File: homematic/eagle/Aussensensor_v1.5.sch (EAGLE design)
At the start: 44 parts, among them IC1 Atmega 328P, IC2 MAX1724, IC3 MAX44009, IC4 TSL256FN, IC5 BMP180, IC6 BME280, IC7 DS18B20, M1 CC1101_WIRELES_MODULE, T1 IRML6344

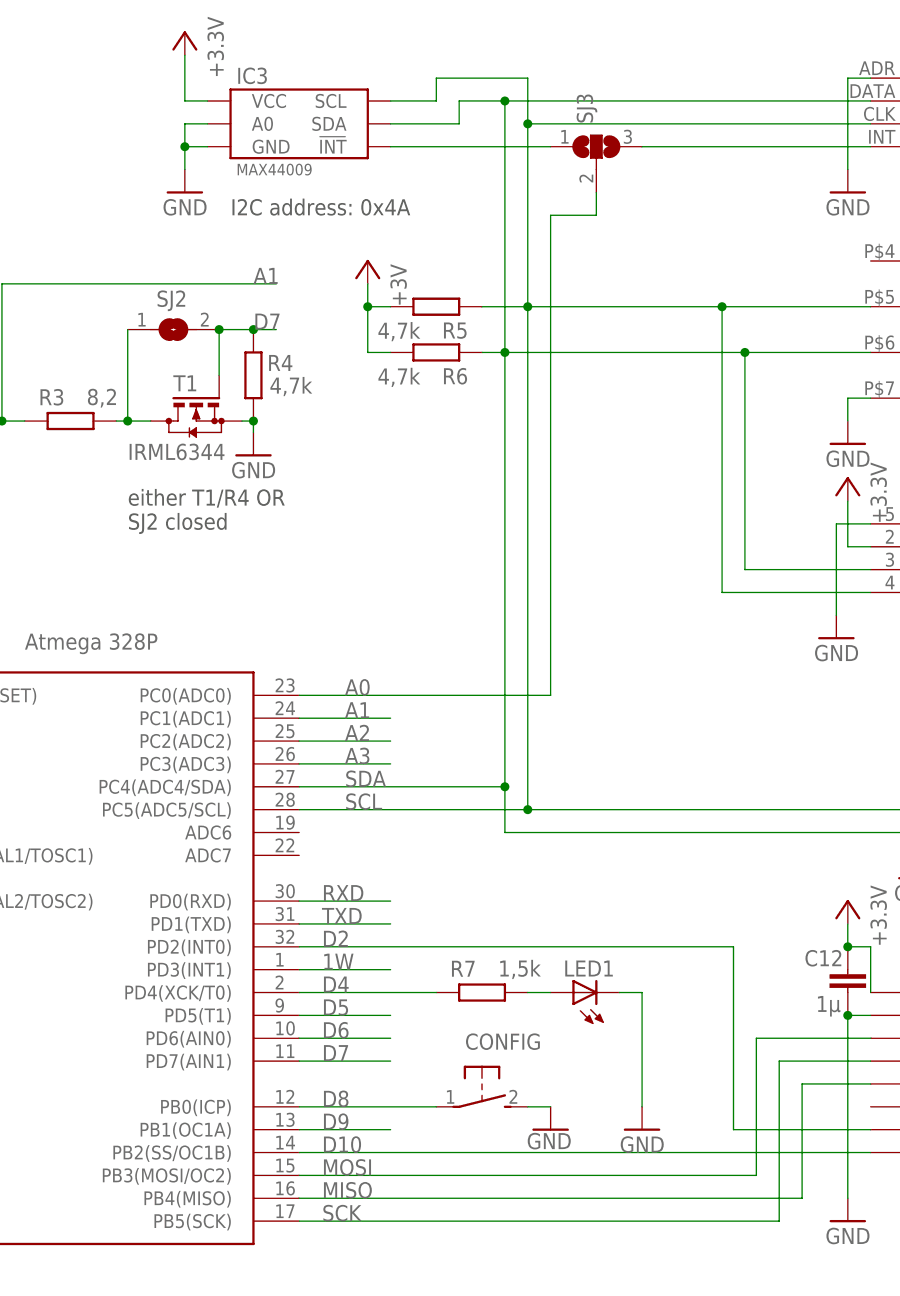
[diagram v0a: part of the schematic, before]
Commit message: Changed compared to previous version: - all vias diameter 0.7, drill 0,4 mm - moved vias for buffer capacitor C3 and C11 - improved layout for C6 - R9 (pull up for CSN) added
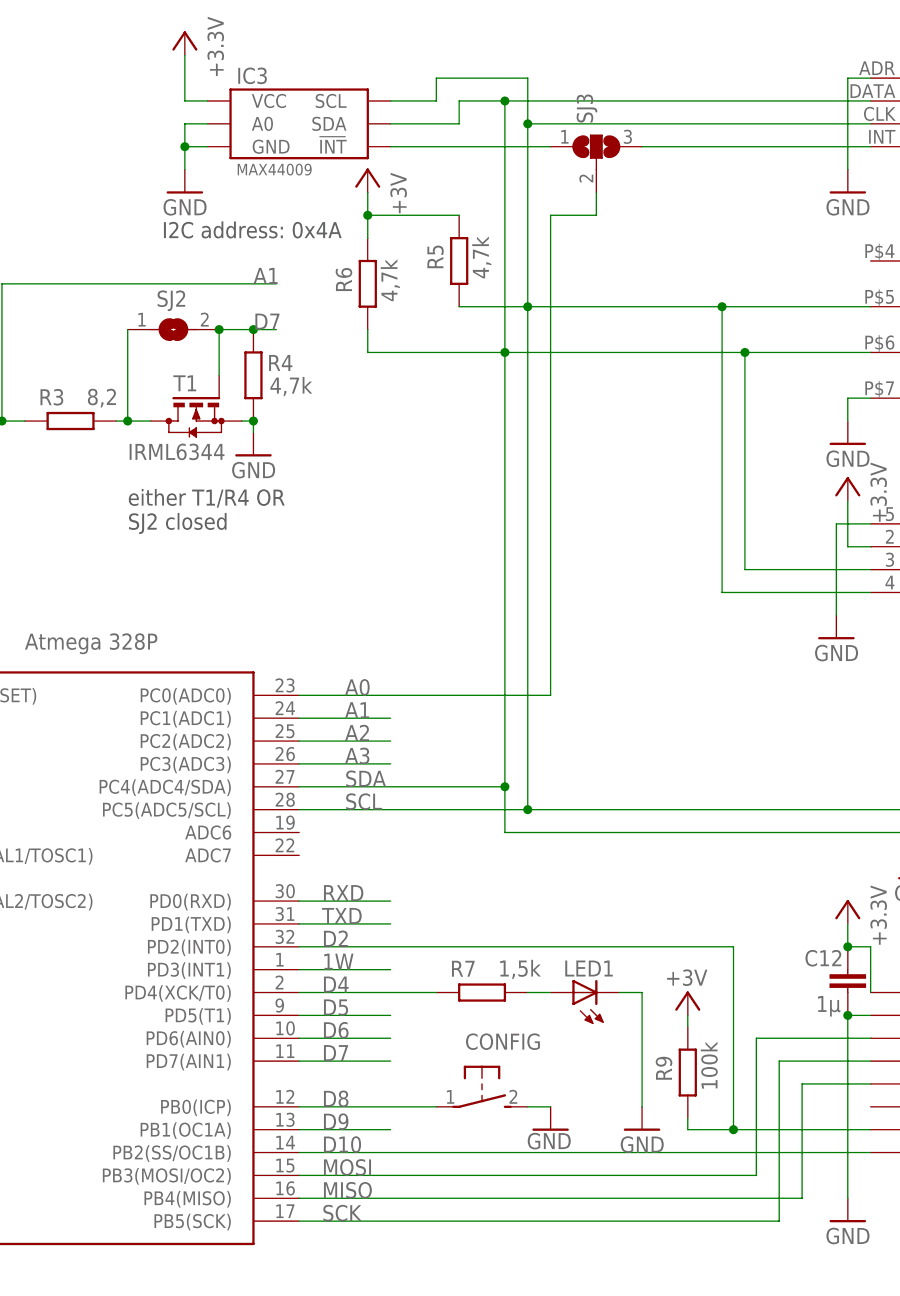
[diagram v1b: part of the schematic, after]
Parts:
- added R9: 100k, rcl:R-EU_M0805
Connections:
- net +3.3V: now also R9.2
- net D2: now also R9.1
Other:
- moved on the sheet: R5, R6
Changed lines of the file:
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@@
 <setting verticaltext="up"/>
 </settings>
-<grid distance="0.1" unitdist="inch" unit="mil" style="lines" multiple="1" display="no" altdistance="0.01" altunitdist="inch" altunit="inch"/>
+<grid distance="50" unitdist="mil" unit="mil" style="lines" multiple="1" display="no" altdistance="0.01" altunitdist="inch" altunit="inch"/>
 <layers>
 <layer number="1" name="Top" color="4" fill="1" visible="no" active="no"/>
@@
 <part name="SJ3" library="jumper" deviceset="SJ2W" device=""/>
 <part name="IC4" library="TSL256x" deviceset="TSL256*" device="FN"/>
+<part name="R9" library="rcl" deviceset="R-EU_" device="M0805" value="100k"/>
+<part name="P+14" library="supply1" deviceset="+5V" device="" value="+3V"/>
 </parts>
 <sheets>
@@
 <text x="120.65" y="124.46" size="1.778" layer="97" rot="MR180">either T1/R4 OR
 SJ2 closed</text>
-<text x="132.08" y="154.94" size="1.778" layer="97">I2C address: 0x4A</text>
+<text x="124.46" y="152.4" size="1.778" layer="97">I2C address: 0x4A</text>
 </plain>
 <instances>
@@
 <instance part="GND15" gate="1" x="254" y="129.54" rot="MR0"/>
 <instance part="GND16" gate="1" x="200.66" y="129.54" rot="MR0"/>
-<instance part="R6" gate="G$1" x="154.94" y="139.7" smashed="yes" rot="R180">
-<attribute name="NAME" x="158.496" y="137.9474" size="1.778" layer="95" rot="R180"/>
-<attribute name="VALUE" x="153.162" y="137.922" size="1.778" layer="96" rot="R180"/>
-</instance>
-<instance part="R5" gate="G$1" x="154.94" y="144.78" smashed="yes" rot="R180">
-<attribute name="NAME" x="158.496" y="143.0274" size="1.778" layer="95" rot="R180"/>
-<attribute name="VALUE" x="153.162" y="143.002" size="1.778" layer="96" rot="R180"/>
-</instance>
-<instance part="P+6" gate="1" x="147.32" y="149.86" rot="MR0"/>
+<instance part="R6" gate="G$1" x="147.32" y="147.32" smashed="yes" rot="R90">
+<attribute name="NAME" x="145.5674" y="146.304" size="1.778" layer="95" rot="R90"/>
+<attribute name="VALUE" x="150.622" y="145.288" size="1.778" layer="96" rot="R90"/>
+</instance>
+<instance part="R5" gate="G$1" x="157.48" y="149.86" smashed="yes" rot="R90">
+<attribute name="NAME" x="155.7274" y="148.844" size="1.778" layer="95" rot="R90"/>
+<attribute name="VALUE" x="160.782" y="147.828" size="1.778" layer="96" rot="R90"/>
+</instance>
+<instance part="P+6" gate="1" x="147.32" y="160.02" rot="MR0"/>
 <instance part="GND18" gate="1" x="236.22" y="157.48" rot="MR0"/>
 <instance part="GND19" gate="1" x="200.66" y="157.48" rot="MR0"/>
@@
 <attribute name="NAME" x="208.28" y="173.99" size="1.778" layer="95" rot="MR0" align="bottom-right"/>
 <attribute name="VALUE" x="228.6" y="157.48" size="1.27" layer="96" rot="MR0"/>
+</instance>
+<instance part="R9" gate="G$1" x="182.88" y="59.69" smashed="yes" rot="R90">
+<attribute name="NAME" x="181.1274" y="58.674" size="1.778" layer="95" rot="R90"/>
+<attribute name="VALUE" x="186.182" y="57.658" size="1.778" layer="96" rot="R90"/>
+</instance>
+<instance part="P+14" gate="1" x="182.88" y="68.58" smashed="yes" rot="MR0">
+<attribute name="VALUE" x="180.34" y="71.12" size="1.778" layer="96" rot="MR180"/>
 </instance>
 </instances>
@@
 <wire x1="187.96" y1="53.34" x2="203.2" y2="53.34" width="0.1524" layer="91"/>
 <label x="142.24" y="73.66" size="1.778" layer="95"/>
+<pinref part="R9" gate="G$1" pin="1"/>
+<wire x1="182.88" y1="54.61" x2="182.88" y2="53.34" width="0.1524" layer="91"/>
+<wire x1="182.88" y1="53.34" x2="187.96" y2="53.34" width="0.1524" layer="91"/>
+<junction x="187.96" y="53.34"/>
 </segment>
 <segment>
@@
 <pinref part="R6" gate="G$1" pin="1"/>
 <wire x1="189.23" y1="139.7" x2="162.56" y2="139.7" width="0.1524" layer="91"/>
-<wire x1="162.56" y1="139.7" x2="160.02" y2="139.7" width="0.1524" layer="91"/>
+<wire x1="162.56" y1="139.7" x2="147.32" y2="139.7" width="0.1524" layer="91"/>
+<wire x1="147.32" y1="139.7" x2="147.32" y2="142.24" width="0.1524" layer="91"/>
 <label x="144.78" y="91.44" size="1.778" layer="95"/>
 <pinref part="IC6" gate="IC" pin="SDI"/>
@@
 <wire x1="139.7" y1="88.9" x2="165.1" y2="88.9" width="0.1524" layer="91"/>
 <pinref part="R5" gate="G$1" pin="1"/>
-<wire x1="165.1" y1="144.78" x2="160.02" y2="144.78" width="0.1524" layer="91"/>
+<wire x1="165.1" y1="144.78" x2="157.48" y2="144.78" width="0.1524" layer="91"/>
 <label x="144.78" y="88.9" size="1.778" layer="95"/>
 <pinref part="IC6" gate="IC" pin="SCK"/>
@@
 <segment>
 <pinref part="R5" gate="G$1" pin="2"/>
-<wire x1="149.86" y1="144.78" x2="147.32" y2="144.78" width="0.1524" layer="91"/>
-<wire x1="147.32" y1="144.78" x2="147.32" y2="139.7" width="0.1524" layer="91"/>
+<wire x1="157.48" y1="154.94" x2="147.32" y2="154.94" width="0.1524" layer="91"/>
+<wire x1="147.32" y1="154.94" x2="147.32" y2="152.4" width="0.1524" layer="91"/>
 <pinref part="R6" gate="G$1" pin="2"/>
-<wire x1="147.32" y1="139.7" x2="149.86" y2="139.7" width="0.1524" layer="91"/>
 <pinref part="P+6" gate="1" pin="+5V"/>
-<wire x1="147.32" y1="144.78" x2="147.32" y2="147.32" width="0.1524" layer="91"/>
-<junction x="147.32" y="144.78"/>
+<wire x1="147.32" y1="154.94" x2="147.32" y2="157.48" width="0.1524" layer="91"/>
+<junction x="147.32" y="154.94"/>
 </segment>
 <segment>
@@
 <wire x1="127" y1="167.64" x2="127" y2="172.72" width="0.1524" layer="91"/>
 </segment>
-</net>
+<segment>
+<pinref part="P+14" gate="1" pin="+5V"/>
+<pinref part="R9" gate="G$1" pin="2"/>
+<wire x1="182.88" y1="66.04" x2="182.88" y2="64.77" width="0.1524" layer="91"/>
+</segment>
+</net>

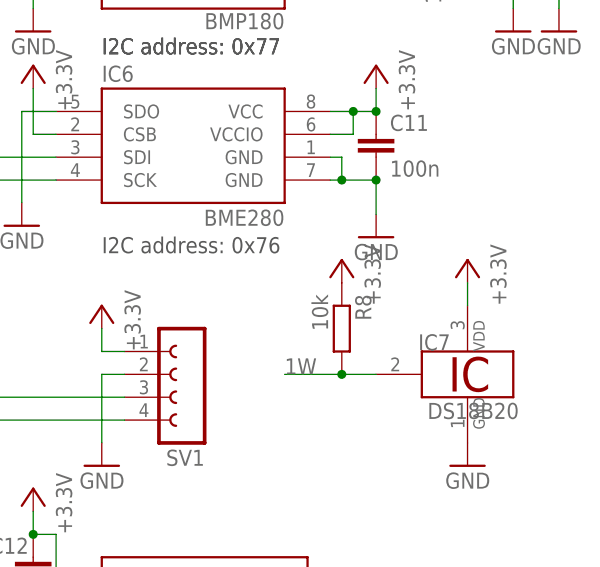
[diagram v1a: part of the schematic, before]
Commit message: replaced 10k by 4k7 for DS18x20 in Aussensensor v1.4 and v1.5
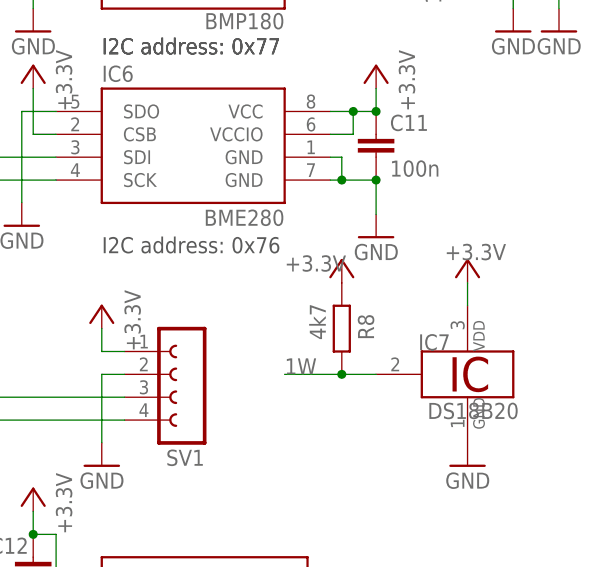
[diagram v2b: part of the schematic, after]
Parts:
- R8: value 10k -> 4k7
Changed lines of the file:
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@@
 <setting verticaltext="up"/>
 </settings>
-<grid distance="50" unitdist="mil" unit="mil" style="lines" multiple="1" display="no" altdistance="0.01" altunitdist="inch" altunit="inch"/>
+<grid distance="0.1" unitdist="inch" unit="inch" style="lines" multiple="1" display="no" altdistance="0.01" altunitdist="inch" altunit="inch"/>
 <layers>
 <layer number="1" name="Top" color="4" fill="1" visible="no" active="no"/>
@@
 <part name="P+11" library="supply1" deviceset="+5V" device="" value="+3.3V"/>
 <part name="GND21" library="supply1" deviceset="GND" device=""/>
-<part name="R8" library="rcl" deviceset="R-EU_" device="M0805" value="10k"/>
+<part name="R8" library="rcl" deviceset="R-EU_" device="M0805" value="4k7"/>
 <part name="P+12" library="supply1" deviceset="+5V" device="" value="+3.3V"/>
 <part name="C12" library="rcl" deviceset="C-EU" device="C0805" value="1µ"/>
@@
 <instance part="IC7" gate="P" x="248.92" y="91.44" smashed="yes"/>
 <instance part="IC7" gate="_1W" x="243.84" y="91.44" smashed="yes"/>
-<instance part="P+11" gate="1" x="248.92" y="104.14" rot="MR0"/>
+<instance part="P+11" gate="1" x="248.92" y="104.14" smashed="yes" rot="MR0">
+<attribute name="VALUE" x="246.38" y="104.14" size="1.778" layer="96"/>
+</instance>
 <instance part="GND21" gate="1" x="248.92" y="81.28" rot="MR0"/>
-<instance part="R8" gate="G$1" x="234.95" y="96.52" rot="R270"/>
-<instance part="P+12" gate="1" x="234.95" y="104.14" rot="MR0"/>
+<instance part="R8" gate="G$1" x="234.95" y="96.52" smashed="yes" rot="R270">
+<attribute name="NAME" x="238.5314" y="95.25" size="1.778" layer="95" rot="R90"/>
+<attribute name="VALUE" x="233.172" y="95.25" size="1.778" layer="96" rot="R90"/>
+</instance>
+<instance part="P+12" gate="1" x="234.95" y="104.14" smashed="yes" rot="MR0">
+<attribute name="VALUE" x="228.6" y="102.87" size="1.778" layer="96"/>
+</instance>
 <instance part="C12" gate="G$1" x="200.66" y="71.12" smashed="yes">
 <attribute name="NAME" x="195.834" y="71.501" size="1.778" layer="95"/>

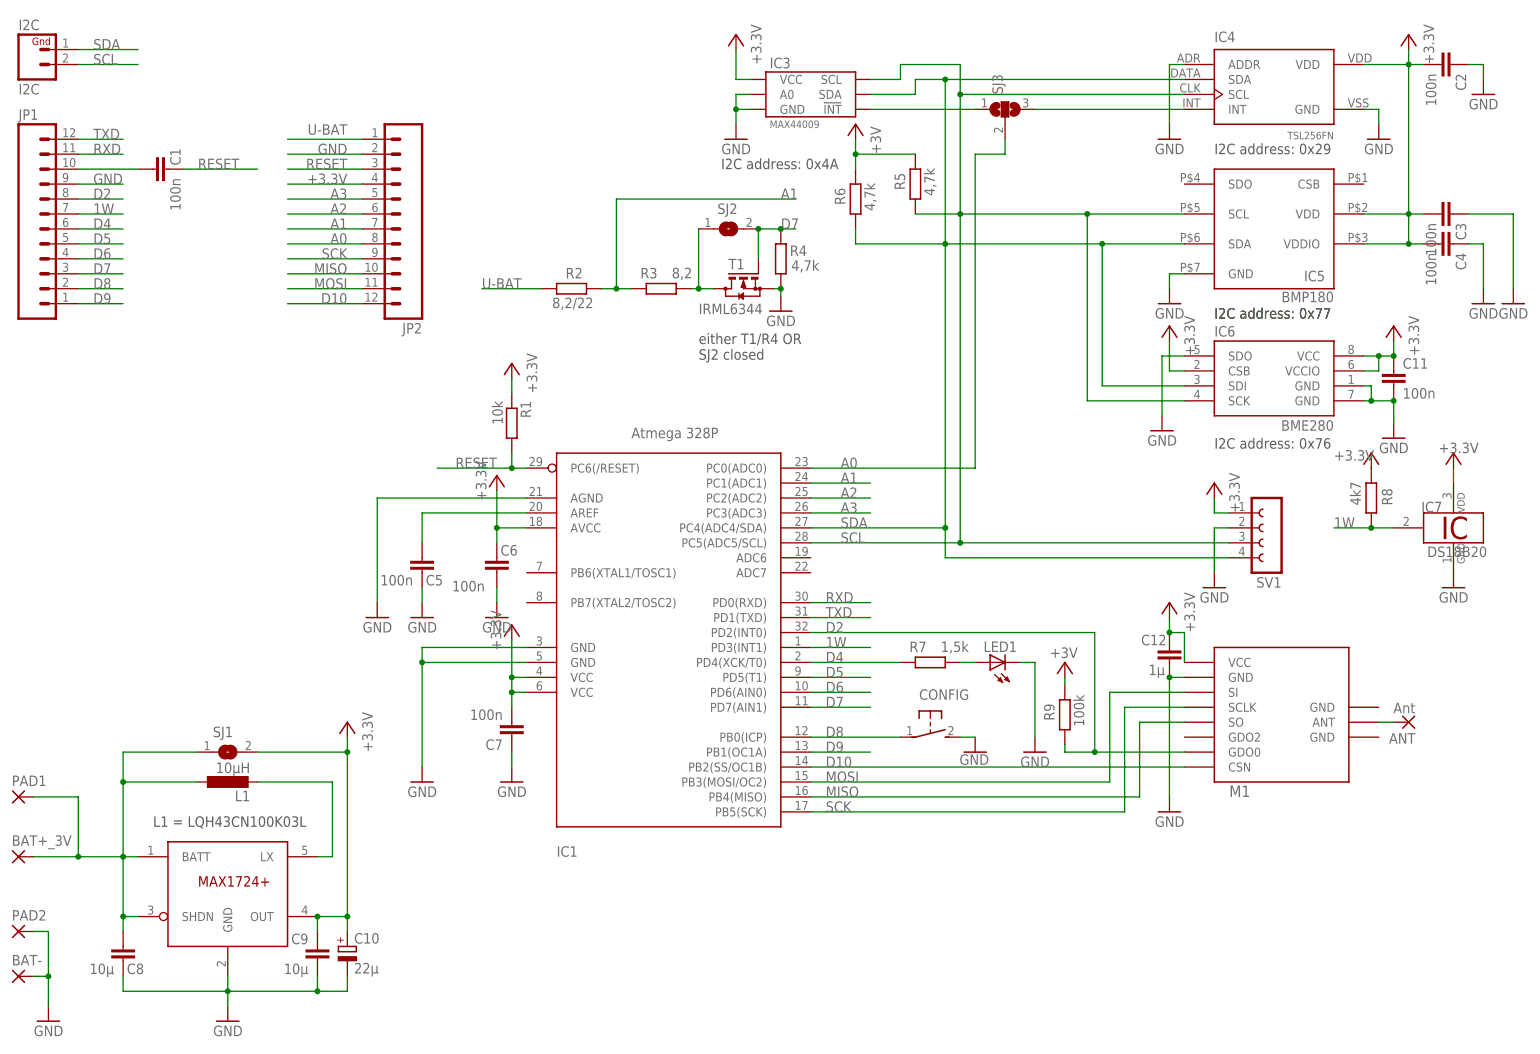
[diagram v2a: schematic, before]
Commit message: replace Aussensensor v1.5 with a better readable schematic (no layout change)
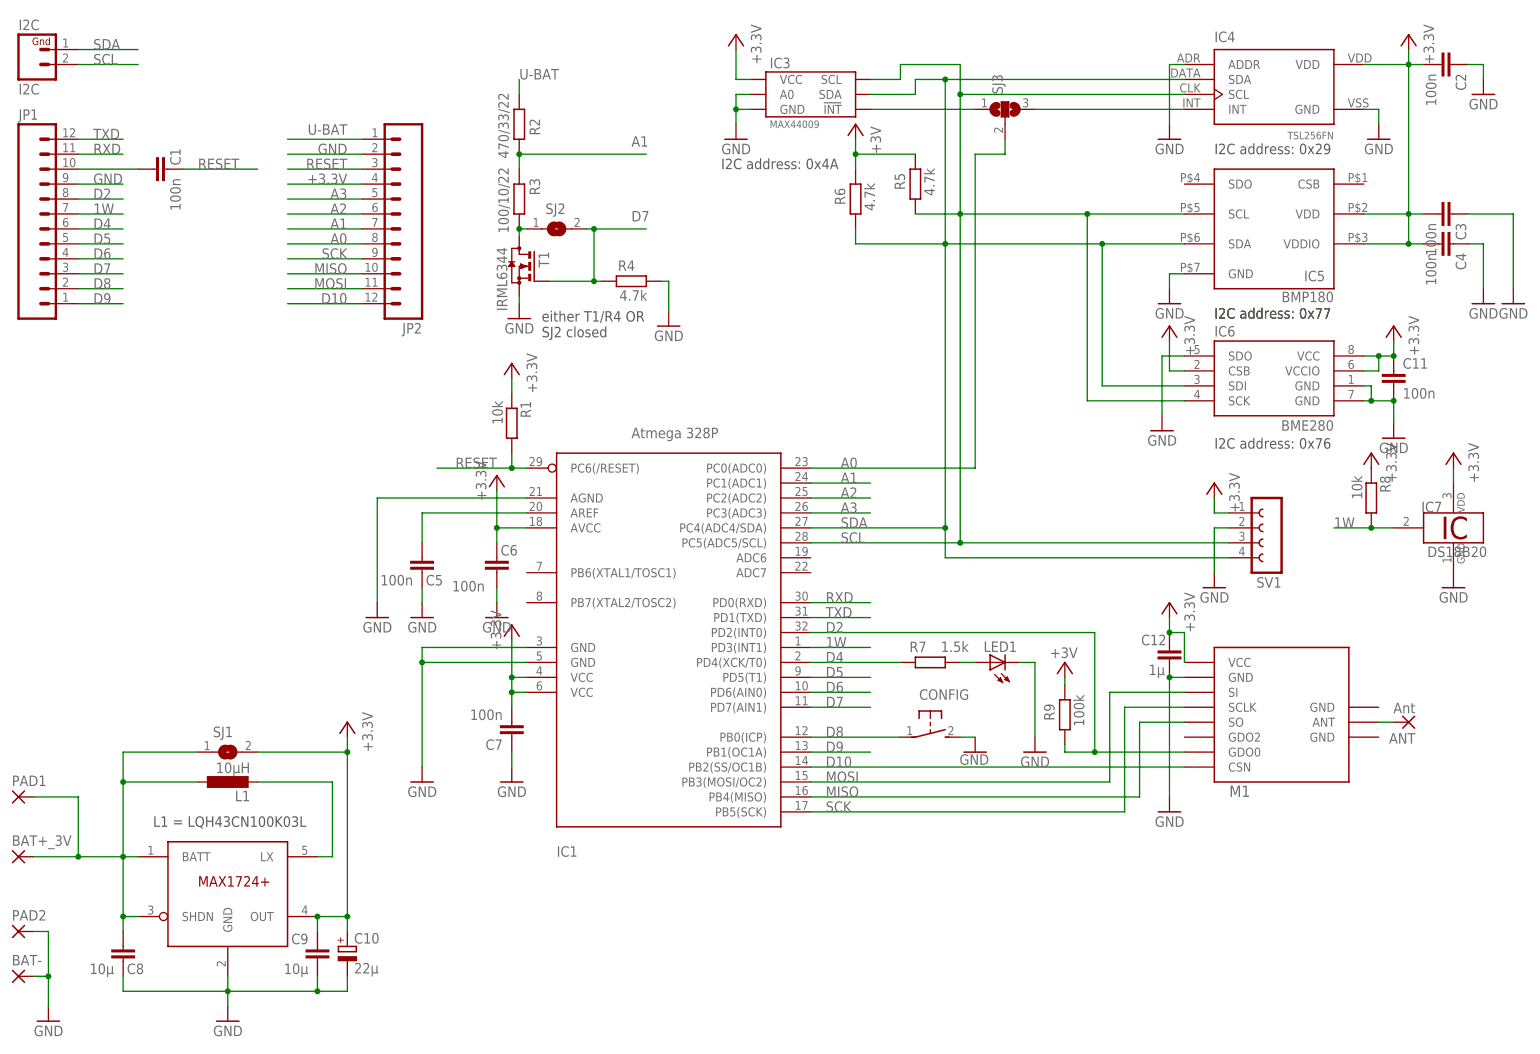
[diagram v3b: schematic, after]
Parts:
- R2: value 8,2/22 -> 470/33/22
- R3: value 8,2 -> 100/10/22
- R4, R5, R6: value 4,7k -> 4.7k
- R7: value 1,5k -> 1.5k
- R8: value 4k7 -> 10k
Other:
- moved on the sheet: R2, R3, R4, SJ2, T1
